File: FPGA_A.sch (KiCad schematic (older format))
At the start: 2 parts, among them CN5 CONN_RCPT_USB2.0_MINI_B_SMD_R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, U15 FT2232HL-REEL

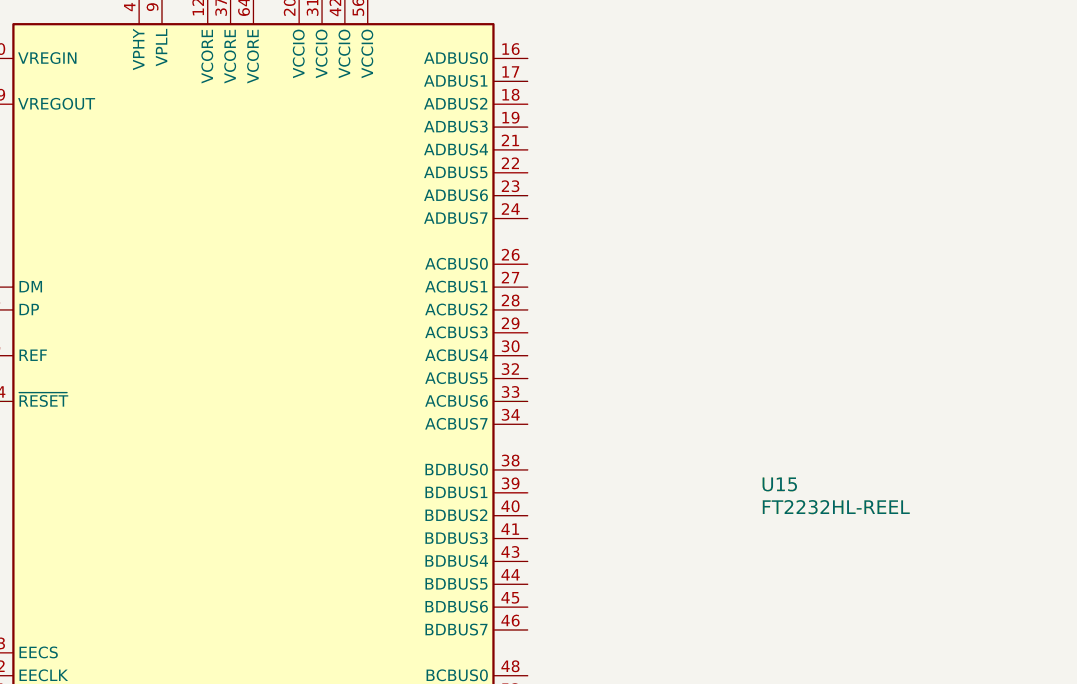
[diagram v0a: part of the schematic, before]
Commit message: Still had some text cleanups to do plus fixed a couple of minor circuit issues.
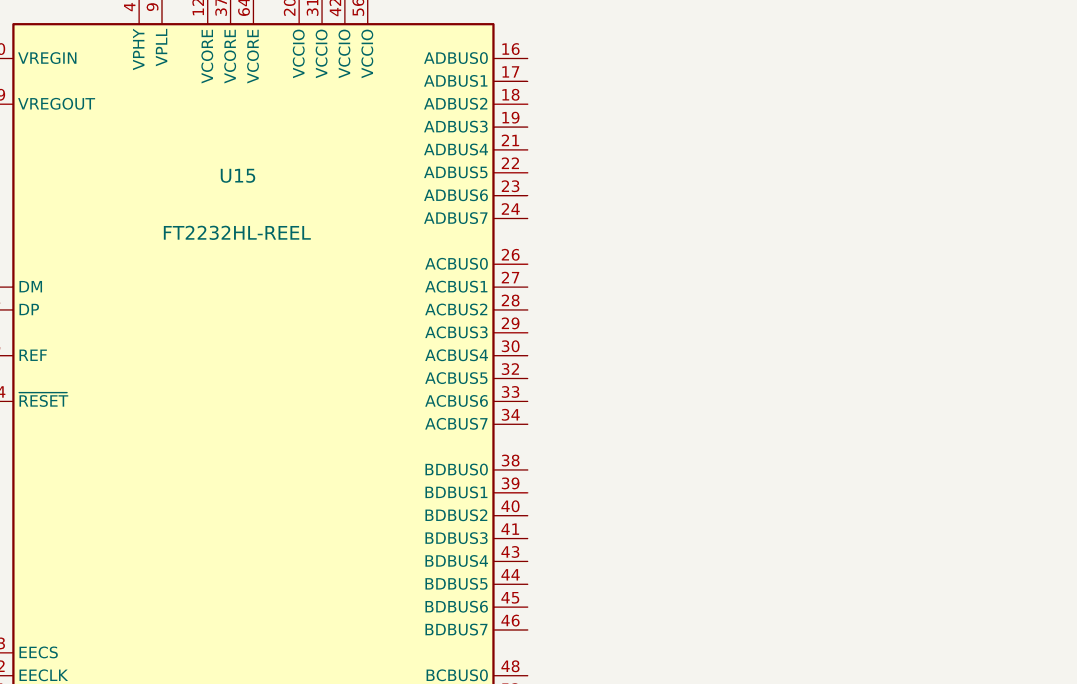
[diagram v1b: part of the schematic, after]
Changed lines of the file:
@@
 U 1 1 5F8DD189
 P 3850 3300
-F 0 "U15" H 6070 3300 60  0000 L BNN
-F 1 "FT2232HL-REEL" H 6070 3200 60  0000 L BNN
+F 0 "U15" H 3700 4650 60  0000 L BNN
+F 1 "FT2232HL-REEL" H 3450 4400 60  0000 L BNN
 F 2 "" H 6070 3200 60  0000 C CNN
 F 3 "" H 6070 3200 60  0000 C CNN
